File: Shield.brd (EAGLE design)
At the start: 53.3 x 58.4 mm, 18 parts, among them Q8 TIP120, U2 ARDUINO_SHIELDNO_SILK

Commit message: Converted to single board
git-svn-id: svn+ssh://petrocik.net/home/svn/repo/uci_gate/branches/hardware/uci_gate/3.x@90 8c868176-b666-4d83-8e7f-acb7c29fc81a
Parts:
- removed R9: 100, SparkFun-Passives:1206
- added C2: 22pf, SparkFun-Capacitors:1206
- added C3: 0.1uf, SparkFun-Capacitors:1206
- added C6: (no value), SparkFun-Capacitors:CAP-PTH-5MM
- added C7, C8: 10uf, SparkFun-Capacitors:CAP-PTH-SMALL
- added J1: AVR_SPI_PRG_6PTH, SparkFun-Connectors:2X3
- added R4: 10K, SparkFun-Passives:1206
- added U4: ATMEGA328P_PDIP, SparkFun-DigitalIC:DIL28-3
- added Y1: 16Mhz, SparkFun-FreqCtrl:HC49US
- C1: value (none) -> 22pf; device SparkFun-Capacitors:CAP-PTH-5MM -> SparkFun-Capacitors:1206
- U2: value ARDUINO_SHIELDNO_SILK -> LM78XX-TO252-3; device SparkFun-Boards:DUEMILANOVE_VIAS -> element14-com:TO252-3
- moved BT_HDR 44.3 mm to (50.8, 27.3), turned to 90 degrees
- moved R1 44.3 mm to (43.8, 27.3)
- moved R2 44.3 mm to (43.8, 24.1), turned to 180 degrees
- moved U2 37.8 mm to (5.08, 50.2)
- moved R10 34.5 mm to (43.8, 21.0)
- moved C1 33.9 mm to (30.5, 50.8), turned to 270 degrees
- moved STRT 27.9 mm to (34.3, 5.08)
- moved U$1 27.4 mm to (31.1, 24.1), turned to 180 degrees
- moved GATE 21.0 mm to (13.3, 5.08)
- moved PWR 21.0 mm to (6.35, 5.08)
- moved TMR 14.0 mm to (27.3, 5.08)
- moved R8 10.3 mm to (17.1, 28.6), turned to 270 degrees
- moved U$2 8.84 mm to (41.3, 50.2), turned to 180 degrees
- moved Q8 5.75 mm to (19.1, 21.6)
- moved R7 5.43 mm to (14.6, 28.6), turned to 90 degrees
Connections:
- net N$6 renamed GATE
- removed net N$1 (its old number): U$1.1, U2.D2
- removed net N$10: LIGHT.7, U$1.16
- removed net N$11: U$2.6, U2.A5
- removed net N$13: R7.2, U2.D9
- removed net N$14: U$2.5, U2.A4
- removed net N$16: BT_HDR.2, U2.RX
- removed net N$18: BT_HDR.4, R8.2, TMR.1, U$2.8, U2.5V
- removed net N$20: R9.1, U2.D12
- removed net N$21: R8.1, R9.2, STRT.1
- removed net N$22: R10.1, TMR.2, U2.A0
- removed net N$23: R1.1, U2.TX
- removed net N$7: LIGHT.1, U$1.13
- removed net N$8: LIGHT.3, U$1.14
- removed net N$9: LIGHT.5, U$1.15
- new net 5V: BT_HDR.4, C3.2, C7.1, J1.2, R4.1, R8.2, TMR.1, U$2.8, U2.3, U4.20, U4.7
- new net A0: R10.1, TMR.2, U4.23
- new net A4: U$2.5, U4.27
- new net A5: U$2.6, U4.28
- new net D2: U$1.1, U4.4
- new net D3: U$1.2, U4.5
- new net D4: U$1.3, U4.6
- new net D5: U$1.4, U4.11
- new net D6: U$1.5, U4.12
- new net D7: R8.1, STRT.1, U4.13
- new net D9: R7.2, U4.15
- new net MISO: J1.1, U4.18
- new net MOSI: J1.4, U4.17
- new net N$15: C1.2, U4.9, Y1.2
- new net N$24: C2.2, U4.10, Y1.1
- new net RESET: J1.5, R4.2, U4.1
- new net RX: BT_HDR.2, U4.2
- new net SCK: J1.3, U4.19
- new net TX: R1.1, U4.3
- net GND: now also C1.1, C2.1, C3.1, C6.2, C7.2, C8.2, J1.6, U2.2, U4.22, U4.8; no longer C1.2, U2.GND@0, U2.GND@1, U2.GND@2
- net N$2: now also LIGHT.1, U$1.16; no longer U$1.2, U2.D3
- net N$3: now also LIGHT.3, U$1.15; no longer U$1.3, U2.D4
- net N$4: now also LIGHT.5, U$1.14; no longer U$1.4, U2.D5
- net N$5: now also LIGHT.7, U$1.13; no longer U$1.5, U2.D6
- net VCC: now also C6.1, C8.1, U2.1; no longer C1.1, U2.VIN
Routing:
- net 5V: track 0.00 -> 142.5 mm
- net N$18: track 121.4 -> 0.00 mm, vias 1 -> 0
- net GND: track 177.0 -> 99.1 mm, vias 0 -> 2
- net N$22: track 67.2 -> 0.00 mm
- net N$9: track 65.8 -> 0.00 mm, vias 1 -> 0
- net N$8: track 63.4 -> 0.00 mm, vias 2 -> 0
- net N$10: track 58.9 -> 0.00 mm, vias 1 -> 0
- net N$7: track 51.8 -> 0.00 mm, vias 2 -> 0
- net D7: track 0.00 -> 47.7 mm
- net RESET: track 0.00 -> 44.9 mm
- net A0: track 0.00 -> 43.5 mm, vias 0 -> 1
- net VCC: track 116.5 -> 143.9 mm, vias 1 -> 0
- net D6: track 0.00 -> 25.1 mm
- net N$21: track 24.9 -> 0.00 mm
- net D5: track 0.00 -> 24.6 mm
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- added copper zone on layer 16, net GND
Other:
- board size 53.3 x 58.4 mm -> 53.3 x 55.9 mm
- board text added: "320"
- board text added: "5v"
- board text added: "Gnd"
- board text added: "Rx"
- board text added: "Tx"
- board text added: "UCI Gate v3.0"
- board text removed: "+ -"
- board text removed: "+5V"
- board text removed: "GND"
- board text removed: "RX"
- board text removed: "TX"
- board text removed: "UCI Gate v2.3"

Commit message: Final 3.0
git-svn-id: svn+ssh://petrocik.net/home/svn/repo/uci_gate/branches/hardware/uci_gate/3.x@91 8c868176-b666-4d83-8e7f-acb7c29fc81a
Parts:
- moved J1 0.63 mm to (5.71, 36.2)
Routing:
- net VCC: track 143.9 -> 149.3 mm
- net SCK: track 19.7 -> 18.9 mm
- net MOSI: track 22.2 -> 23.0 mm
- net MISO: track 16.4 -> 17.2 mm
- net RESET: track 44.9 -> 44.2 mm
- net 5V: track 142.5 -> 143.0 mm

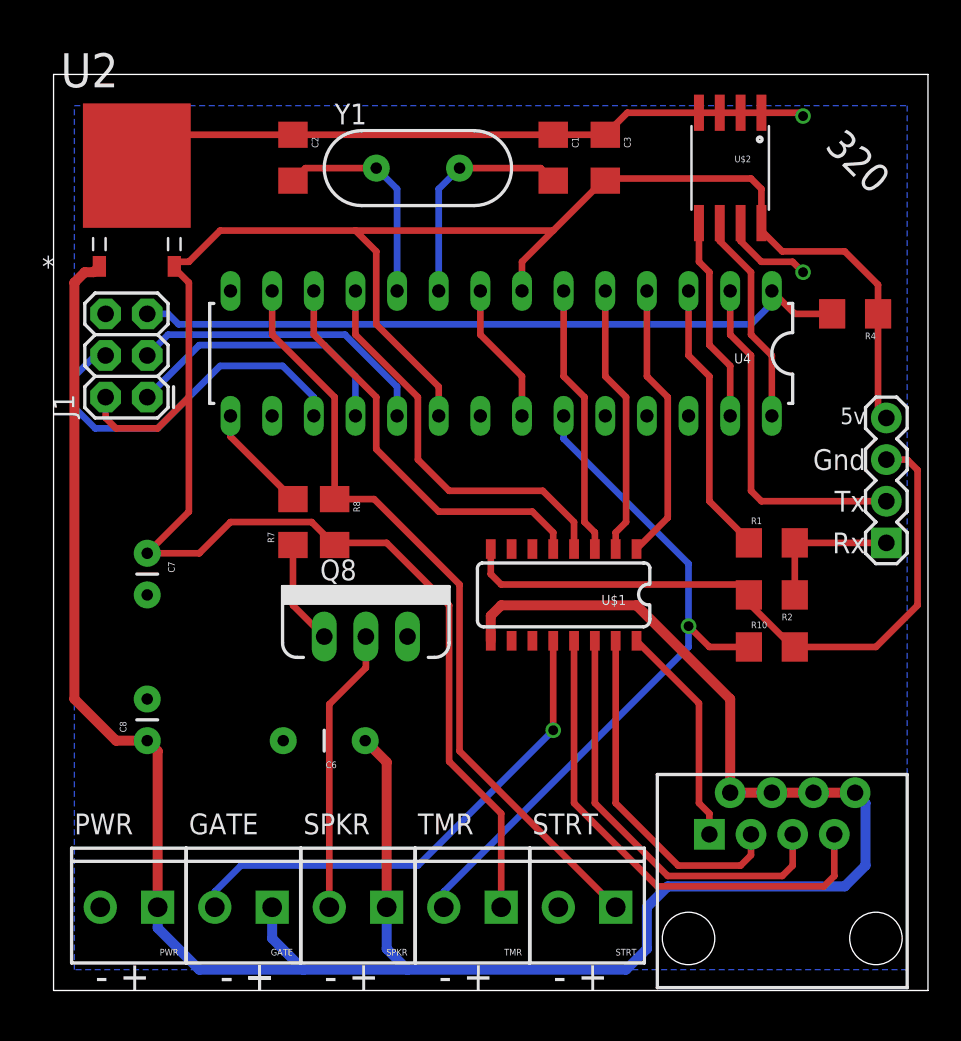
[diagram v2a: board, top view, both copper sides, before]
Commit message: Improvement component placement
git-svn-id: svn+ssh://petrocik.net/home/svn/repo/uci_gate/branches/hardware/uci_gate/3.x@94 8c868176-b666-4d83-8e7f-acb7c29fc81a
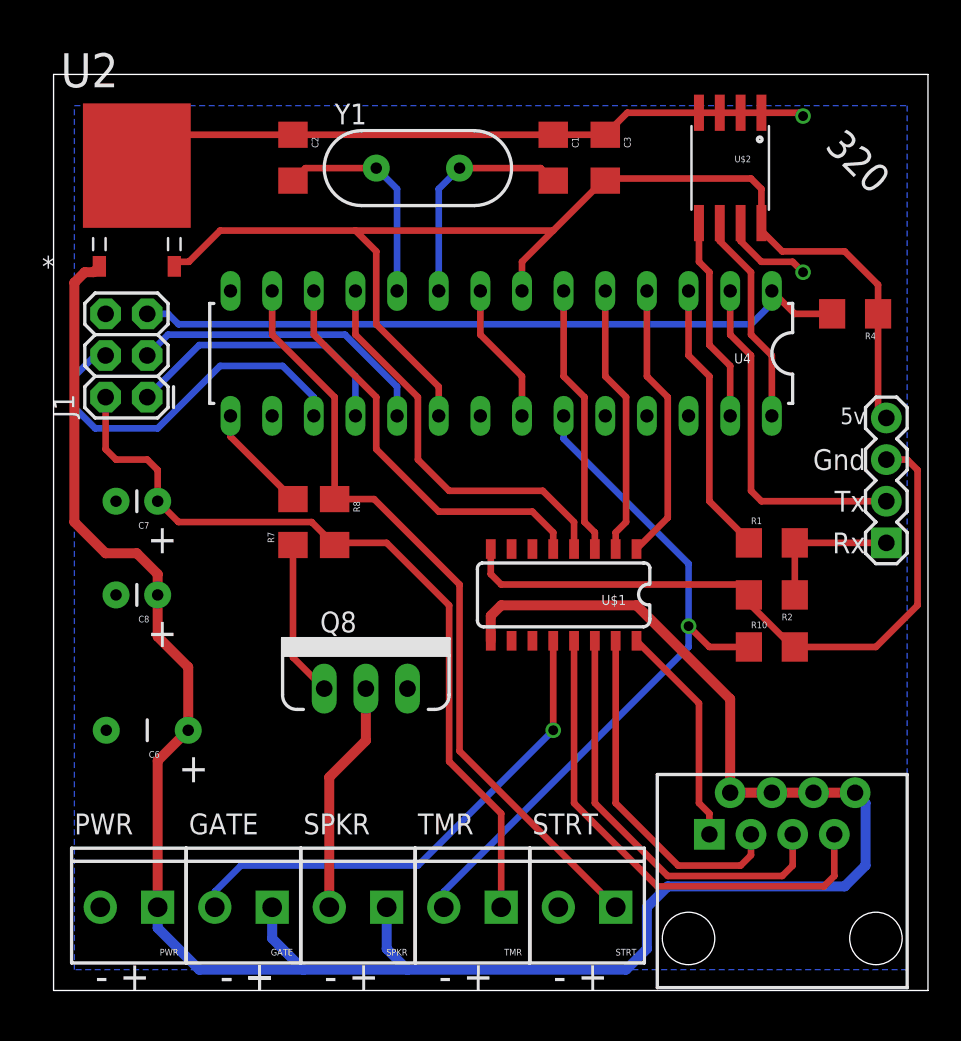
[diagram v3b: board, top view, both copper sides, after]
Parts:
- C6: value (none) -> 1500uf
- moved C6 10.8 mm to (5.71, 15.9)
- moved C8 8.91 mm to (6.35, 24.1), turned to 180 degrees
- moved C7 3.24 mm to (6.35, 29.8), turned to 180 degrees
- moved Q8 3.18 mm to (19.1, 18.4)
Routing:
- net 5V: track 143.0 -> 124.6 mm
- net VCC: track 149.3 -> 140.2 mm
- net N$19: track 6.37 -> 9.55 mm
- net N$12: track 17.4 -> 14.3 mm
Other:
- board text added: "+"
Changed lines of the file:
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@@
 <text x="49.53" y="35.56" size="1.016" layer="21" rot="R180">5v</text>
 <text x="46.99" y="51.435" size="1.778" layer="21" rot="R315">320</text>
+<text x="5.715" y="20.955" size="1.778" layer="21">+</text>
+<text x="5.715" y="26.67" size="1.778" layer="21">+</text>
+<text x="7.62" y="12.7" size="1.778" layer="21">+</text>
 </plain>
 <attributes>
@@
 <element name="PWR" library="SparkFun-Connectors" package="SCREWTERMINAL-3.5MM-2" value="12V" x="6.35" y="5.08" rot="R180"/>
 <element name="SPKR" library="SparkFun-Connectors" package="SCREWTERMINAL-3.5MM-2" value="" x="20.32" y="5.08" rot="R180"/>
-<element name="Q8" library="ucigate" package="TO220V" value="TIP120" x="19.05" y="21.59"/>
+<element name="Q8" library="ucigate" package="TO220V" value="TIP120" x="19.05" y="18.415"/>
 <element name="R8" library="SparkFun-Passives" package="1206" value="10K" x="17.145" y="28.575" rot="R270"/>
 <element name="STRT" library="SparkFun-Connectors" package="SCREWTERMINAL-3.5MM-2" value="" x="34.29" y="5.08" rot="R180"/>
@@
 <element name="R1" library="SparkFun-Passives" package="1206" value="1K" x="43.815" y="27.305"/>
 <element name="R2" library="SparkFun-Passives" package="1206" value="2K" x="43.815" y="24.13" rot="R180"/>
-<element name="C6" library="SparkFun-Capacitors" package="CAP-PTH-5MM" value="" x="16.51" y="15.24" rot="R180"/>
+<element name="C6" library="SparkFun-Capacitors" package="CAP-PTH-5MM" value="1500uf" x="5.715" y="15.875" rot="R180"/>
 <element name="Y1" library="SparkFun-FreqCtrl" package="HC49US" value="16Mhz" x="22.225" y="50.165"/>
 <element name="C1" library="SparkFun-Capacitors" package="1206" value="22pf" x="30.48" y="50.8" rot="R270"/>
 <element name="C2" library="SparkFun-Capacitors" package="1206" value="22pf" x="14.605" y="50.8" rot="R270"/>
 <element name="C3" library="SparkFun-Capacitors" package="1206" value="0.1uf" x="33.655" y="50.8" rot="R270"/>
-<element name="C7" library="SparkFun-Capacitors" package="CAP-PTH-SMALL" value="10uf" x="5.715" y="26.67" rot="R270"/>
-<element name="C8" library="SparkFun-Capacitors" package="CAP-PTH-SMALL" value="10uf" x="5.715" y="15.24" rot="R90"/>
+<element name="C7" library="SparkFun-Capacitors" package="CAP-PTH-SMALL" value="10uf" x="6.35" y="29.845" rot="R180"/>
+<element name="C8" library="SparkFun-Capacitors" package="CAP-PTH-SMALL" value="10uf" x="6.35" y="24.13" rot="R180"/>
 <element name="J1" library="SparkFun-Connectors" package="2X3" value="AVR_SPI_PRG_6PTH" x="5.715" y="36.195" rot="R90"/>
 <element name="R4" library="SparkFun-Passives" package="1206" value="10K" x="48.895" y="41.275" rot="R180"/>
@@
 <contactref element="U2" pad="1"/>
 <wire x1="41.275" y1="12.065" x2="41.275" y2="17.78" width="0.6096" layer="1"/>
-<wire x1="5.715" y1="15.24" x2="6.35" y2="14.605" width="0.6096" layer="1"/>
-<wire x1="6.35" y1="14.605" x2="6.35" y2="5.08" width="0.6096" layer="1"/>
-<wire x1="19.01" y1="15.24" x2="20.32" y2="13.93" width="0.6096" layer="1"/>
-<wire x1="20.32" y1="13.93" x2="20.32" y2="5.08" width="0.6096" layer="1"/>
 <wire x1="6.35" y1="5.08" x2="6.35" y2="3.81" width="0.6096" layer="16"/>
 <wire x1="6.35" y1="3.81" x2="8.89" y2="1.27" width="0.6096" layer="16"/>
@@
 <wire x1="46.355" y1="12.065" x2="43.815" y2="12.065" width="0.6096" layer="1"/>
 <wire x1="43.815" y1="12.065" x2="41.275" y2="12.065" width="0.6096" layer="1"/>
-<wire x1="5.715" y1="15.24" x2="3.81" y2="15.24" width="0.6096" layer="1"/>
-<wire x1="3.81" y1="15.24" x2="1.27" y2="17.78" width="0.6096" layer="1"/>
-<wire x1="1.27" y1="17.78" x2="1.27" y2="43.18" width="0.6096" layer="1"/>
 <wire x1="1.27" y1="43.18" x2="1.905" y2="43.815" width="0.6096" layer="1"/>
 <wire x1="1.905" y1="43.815" x2="2.4384" y2="43.815" width="0.6096" layer="1"/>
@@
 <wire x1="27.305" y1="23.495" x2="35.56" y2="23.495" width="0.6096" layer="1"/>
 <wire x1="35.56" y1="23.495" x2="41.275" y2="17.78" width="0.6096" layer="1"/>
+<wire x1="6.35" y1="24.13" x2="6.35" y2="25.4" width="0.6096" layer="1"/>
+<wire x1="6.35" y1="25.4" x2="5.08" y2="26.67" width="0.6096" layer="1"/>
+<wire x1="5.08" y1="26.67" x2="3.175" y2="26.67" width="0.6096" layer="1"/>
+<wire x1="3.175" y1="26.67" x2="1.27" y2="28.575" width="0.6096" layer="1"/>
+<wire x1="1.27" y1="28.575" x2="1.27" y2="43.18" width="0.6096" layer="1"/>
+<wire x1="6.35" y1="5.08" x2="6.35" y2="14.01" width="0.6096" layer="1"/>
+<wire x1="6.35" y1="14.01" x2="8.215" y2="15.875" width="0.6096" layer="1"/>
+<wire x1="8.215" y1="15.875" x2="8.215" y2="19.725" width="0.6096" layer="1"/>
+<wire x1="8.215" y1="19.725" x2="6.35" y2="21.59" width="0.6096" layer="1"/>
+<wire x1="6.35" y1="21.59" x2="6.35" y2="24.13" width="0.6096" layer="1"/>
 </signal>
 <signal name="D7">
@@
 <contactref element="SPKR" pad="2"/>
 <contactref element="Q8" pad="2"/>
-<wire x1="19.05" y1="21.59" x2="19.05" y2="20.955" width="0.4064" layer="1"/>
-<wire x1="19.05" y1="20.955" x2="19.05" y2="20.32" width="0.4064" layer="1"/>
-<wire x1="16.82" y1="5.08" x2="16.82" y2="17.455" width="0.4064" layer="1"/>
-<wire x1="16.82" y1="17.455" x2="19.05" y2="19.685" width="0.4064" layer="1"/>
-<wire x1="19.05" y1="19.685" x2="19.05" y2="20.32" width="0.4064" layer="1"/>
+<wire x1="16.82" y1="5.08" x2="16.82" y2="13.01" width="0.6096" layer="1"/>
+<wire x1="16.82" y1="13.01" x2="19.05" y2="15.24" width="0.6096" layer="1"/>
+<wire x1="19.05" y1="15.24" x2="19.05" y2="18.415" width="0.6096" layer="1"/>
 </signal>
 <signal name="N$19">
 <contactref element="R7" pad="1"/>
 <contactref element="Q8" pad="1"/>
-<wire x1="16.51" y1="21.59" x2="14.605" y2="23.495" width="0.4064" layer="1"/>
-<wire x1="14.605" y1="23.495" x2="14.605" y2="27.175" width="0.4064" layer="1"/>
+<wire x1="14.605" y1="27.175" x2="14.605" y2="20.32" width="0.4064" layer="1"/>
+<wire x1="14.605" y1="20.32" x2="16.51" y2="18.415" width="0.4064" layer="1"/>
 </signal>
 <signal name="N$15">
@@
 <wire x1="20.32" y1="27.305" x2="17.275" y2="27.305" width="0.4064" layer="1"/>
 <wire x1="17.275" y1="27.305" x2="17.145" y2="27.175" width="0.4064" layer="1"/>
-<wire x1="5.715" y1="26.67" x2="8.89" y2="26.67" width="0.4064" layer="1"/>
-<wire x1="8.89" y1="26.67" x2="10.795" y2="28.575" width="0.4064" layer="1"/>
-<wire x1="10.795" y1="28.575" x2="15.745" y2="28.575" width="0.4064" layer="1"/>
+<wire x1="7.62" y1="28.575" x2="15.745" y2="28.575" width="0.4064" layer="1"/>
 <wire x1="15.745" y1="28.575" x2="17.145" y2="27.175" width="0.4064" layer="1"/>
-<wire x1="7.366" y1="44.1706" x2="7.366" y2="44.069" width="0.4064" layer="1"/>
-<wire x1="7.366" y1="44.069" x2="8.255" y2="43.18" width="0.4064" layer="1"/>
-<wire x1="8.255" y1="43.18" x2="8.255" y2="36.195" width="0.4064" layer="1"/>
-<wire x1="8.255" y1="36.195" x2="8.255" y2="29.21" width="0.4064" layer="1"/>
-<wire x1="8.255" y1="29.21" x2="5.715" y2="26.67" width="0.4064" layer="1"/>
-<wire x1="3.175" y1="36.195" x2="3.175" y2="34.925" width="0.4064" layer="1"/>
-<wire x1="3.175" y1="34.925" x2="3.81" y2="34.29" width="0.4064" layer="1"/>
-<wire x1="3.81" y1="34.29" x2="6.35" y2="34.29" width="0.4064" layer="1"/>
-<wire x1="6.35" y1="34.29" x2="8.255" y2="36.195" width="0.4064" layer="1"/>
+<wire x1="6.35" y1="29.845" x2="7.62" y2="28.575" width="0.4064" layer="1"/>
+<wire x1="6.35" y1="29.845" x2="6.35" y2="31.75" width="0.4064" layer="1"/>
+<wire x1="6.35" y1="31.75" x2="5.715" y2="32.385" width="0.4064" layer="1"/>
+<wire x1="5.715" y1="32.385" x2="3.81" y2="32.385" width="0.4064" layer="1"/>
+<wire x1="3.81" y1="32.385" x2="3.175" y2="33.02" width="0.4064" layer="1"/>
+<wire x1="3.175" y1="33.02" x2="3.175" y2="36.195" width="0.4064" layer="1"/>
+<wire x1="20.32" y1="27.305" x2="23.495" y2="35.052" width="0" layer="19" extent="1-1"/>
 </signal>
 <signal name="D2">

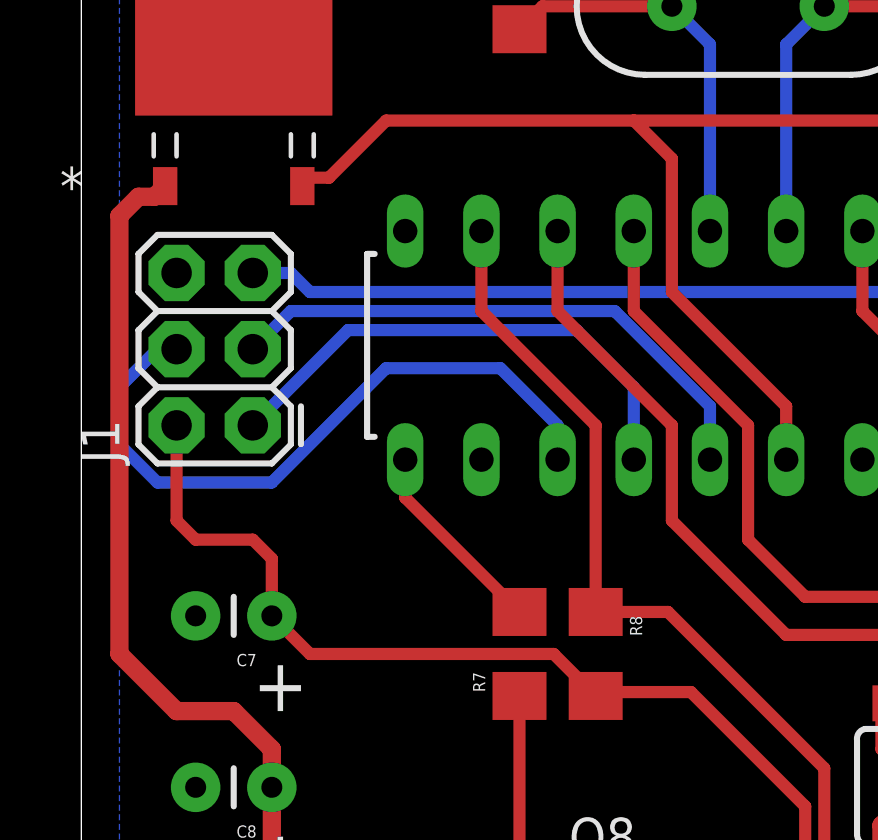
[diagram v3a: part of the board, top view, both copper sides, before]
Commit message: Added missing trace
git-svn-id: svn+ssh://petrocik.net/home/svn/repo/uci_gate/branches/hardware/uci_gate/3.x@95 8c868176-b666-4d83-8e7f-acb7c29fc81a
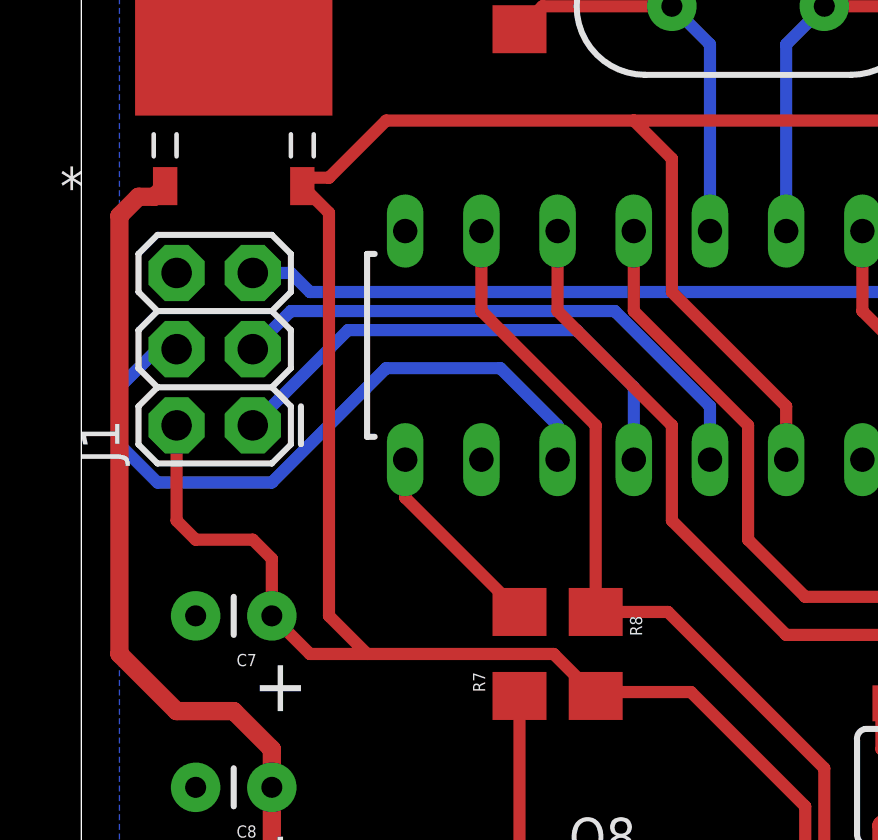
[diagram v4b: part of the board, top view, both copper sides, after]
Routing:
- net 5V: track 124.6 -> 141.1 mm
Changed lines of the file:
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@@
 <wire x1="20.32" y1="27.305" x2="17.275" y2="27.305" width="0.4064" layer="1"/>
 <wire x1="17.275" y1="27.305" x2="17.145" y2="27.175" width="0.4064" layer="1"/>
-<wire x1="7.62" y1="28.575" x2="15.745" y2="28.575" width="0.4064" layer="1"/>
+<wire x1="7.62" y1="28.575" x2="9.525" y2="28.575" width="0.4064" layer="1"/>
+<wire x1="9.525" y1="28.575" x2="15.745" y2="28.575" width="0.4064" layer="1"/>
 <wire x1="15.745" y1="28.575" x2="17.145" y2="27.175" width="0.4064" layer="1"/>
 <wire x1="6.35" y1="29.845" x2="7.62" y2="28.575" width="0.4064" layer="1"/>
@@
 <wire x1="3.81" y1="32.385" x2="3.175" y2="33.02" width="0.4064" layer="1"/>
 <wire x1="3.175" y1="33.02" x2="3.175" y2="36.195" width="0.4064" layer="1"/>
-<wire x1="20.32" y1="27.305" x2="23.495" y2="35.052" width="0" layer="19" extent="1-1"/>
+<wire x1="7.366" y1="44.1706" x2="8.255" y2="43.2816" width="0.4064" layer="1"/>
+<wire x1="8.255" y1="43.2816" x2="8.255" y2="29.845" width="0.4064" layer="1"/>
+<wire x1="8.255" y1="29.845" x2="9.525" y2="28.575" width="0.4064" layer="1"/>
 </signal>
 <signal name="D2">
